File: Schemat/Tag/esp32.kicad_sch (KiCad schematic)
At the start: 30 parts, among them J4 Conn_01x02_Pin, J5 Conn_01x04_Pin, J6 Conn_01x02_Pin, J7 Conn_01x02_Pin, SW1 SW_Push, SW4 SW_Push, U7 ESP32-S3-WROOM-1

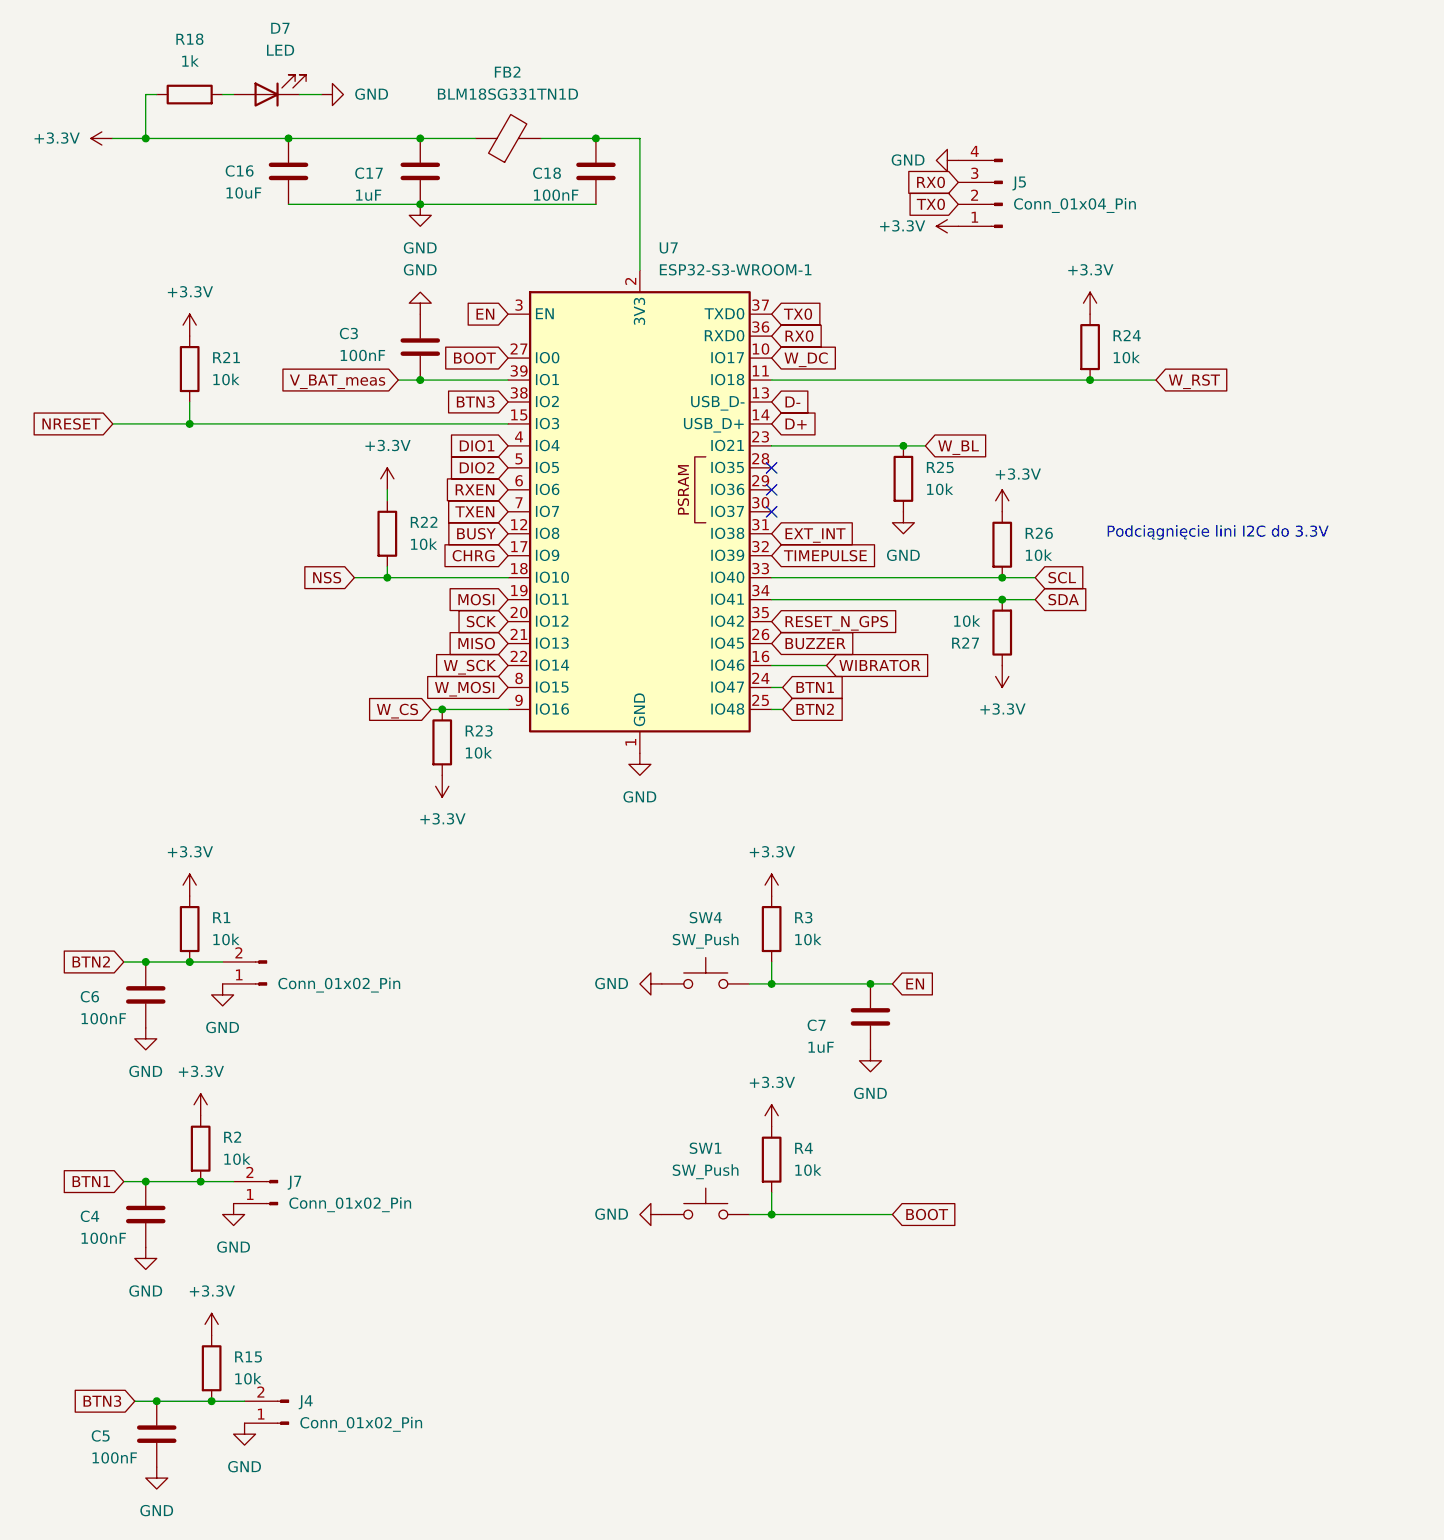
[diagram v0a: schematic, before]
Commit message: Poprawki 09.05
Zmiana poprowadzenia ścieżek sygnałowych w celu poprawy wylewki GND
Dodatkowe przelotki przy GND układy TPS631000
Dodanie zworek 0R z miedzią na wierzchu dla większości linii sygnałowych (nie dodano dla ścieżek do przycisków, bo tam są pady)
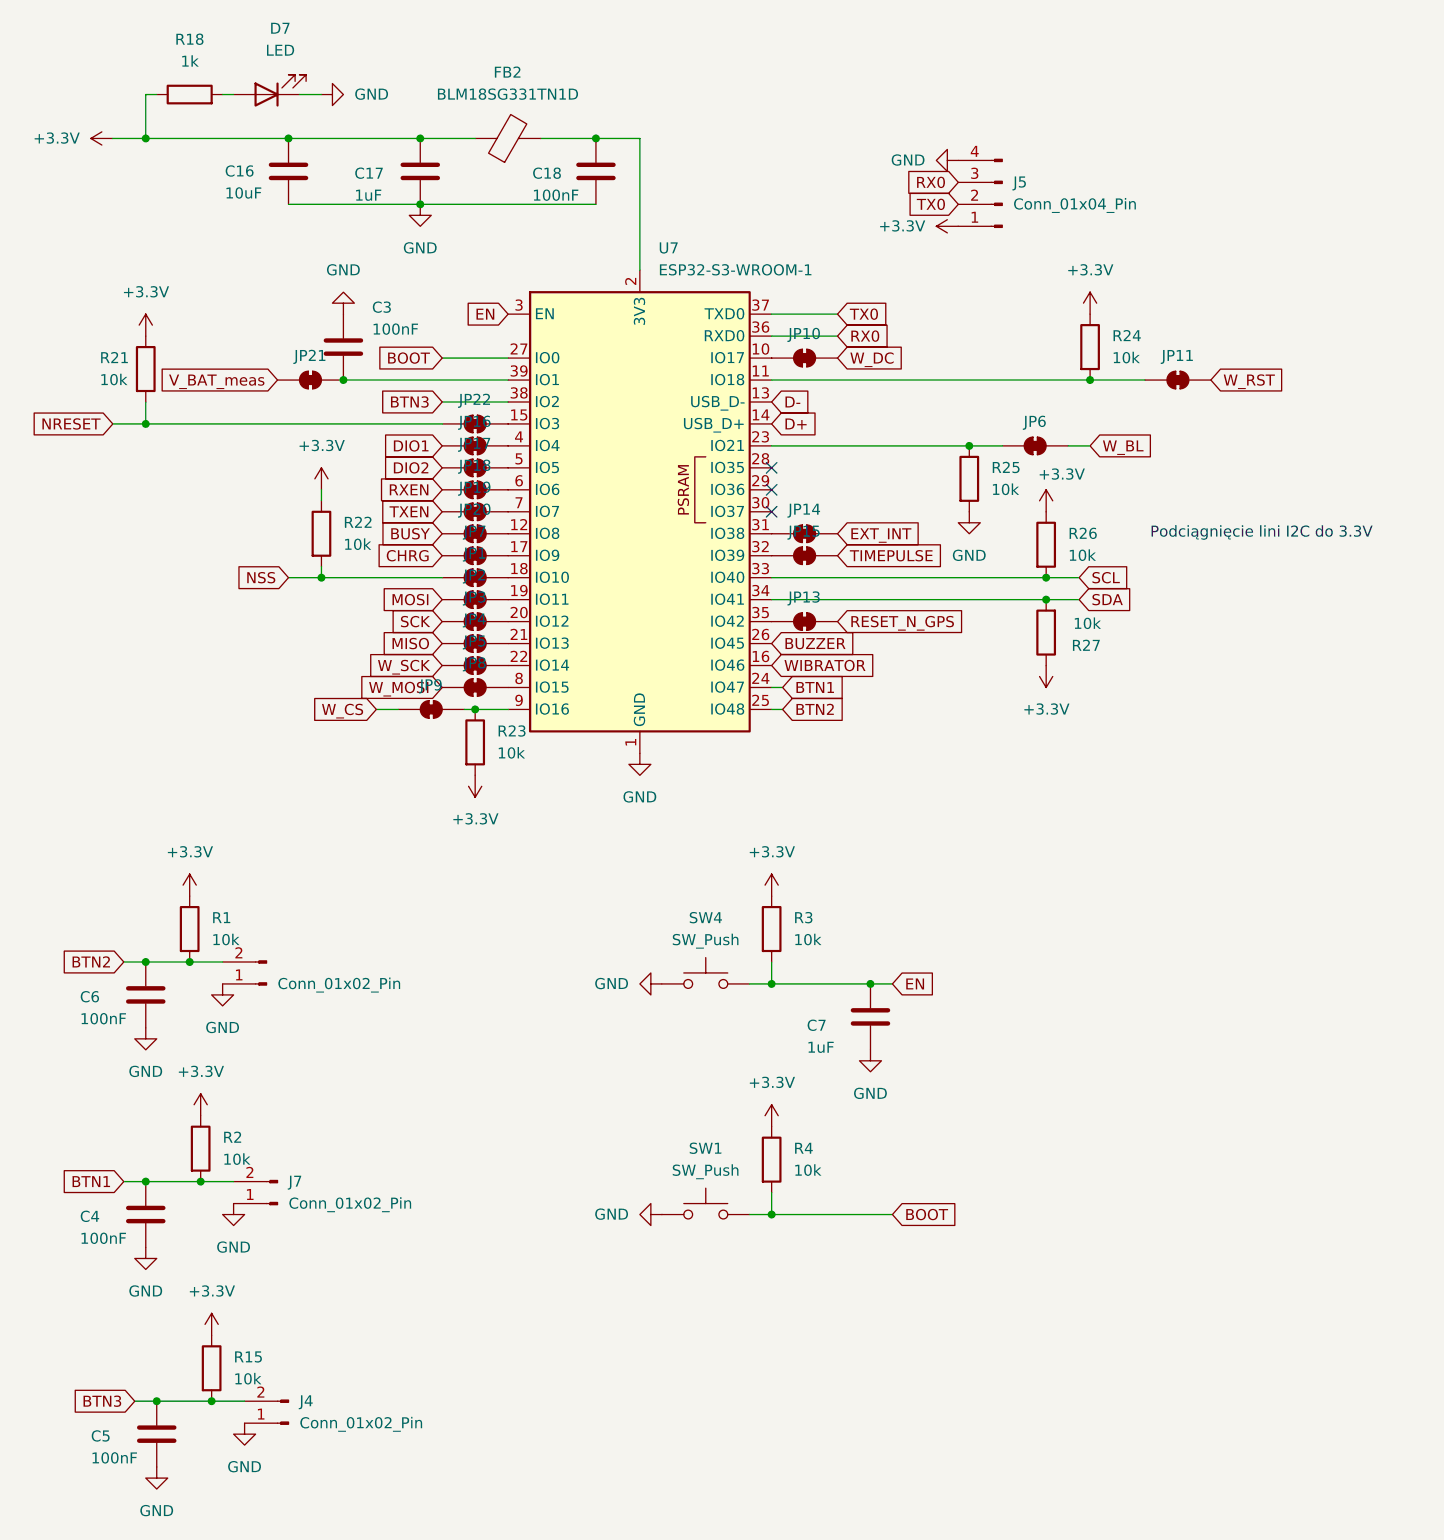
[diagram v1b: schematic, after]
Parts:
- added JP1, JP10, JP11, JP13, JP14, JP15, JP16, JP17, JP18, JP19, JP2, JP20, JP21, JP22, JP3, JP4, JP5, JP6, JP7, JP8, JP9: SolderJumper_2_Bridged, Biblioteka:Zworka, symbol Jumper:SolderJumper_2_Bridged
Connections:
- net BUSY: now also JP20.1 (A); no longer U7.12 (IO8)
- net CHRG: now also JP7.1 (A); no longer U7.17 (IO9)
- net DIO1: now also JP16.1 (A); no longer U7.4 (IO4)
- net DIO2: now also JP17.1 (A); no longer U7.5 (IO5)
- net EXT_INT: now also JP14.2 (B); no longer U7.31 (IO38)
- net MISO: now also JP4.1 (A); no longer U7.21 (IO13)
- net MOSI: now also JP2.1 (A); no longer U7.19 (IO11)
- net NRESET: now also JP22.1 (A); no longer U7.15 (IO3)
- net NSS: now also JP1.1 (A); no longer U7.18 (IO10)
- net RESET_N_GPS: now also JP13.2 (B); no longer U7.35 (IO42)
- net RXEN: now also JP18.1 (A); no longer U7.6 (IO6)
- net SCK: now also JP3.1 (A); no longer U7.20 (IO12)
- net TIMEPULSE: now also JP15.2 (B); no longer U7.32 (IO39)
- net TXEN: now also JP19.1 (A); no longer U7.7 (IO7)
- net V_BAT_meas: now also JP21.1 (A); no longer C3.1, U7.39 (IO1)
- net W_BL: now also JP6.2 (B); no longer R25.1, U7.23 (IO21)
- net W_CS: now also JP9.1 (A); no longer R23.1, U7.9 (IO16)
- net W_DC: now also JP10.2 (B); no longer U7.10 (IO17)
- net W_MOSI: now also JP8.1 (A); no longer U7.8 (IO15)
- net W_RST: now also JP11.2 (B); no longer R24.2, U7.11 (IO18)
- net W_SCK: now also JP5.1 (A); no longer U7.22 (IO14)
- new net: JP11.1 (A), R24.2, U7.11 (IO18)
- new net: JP19.2 (B), U7.7 (IO7)
- new net: JP9.2 (B), R23.1, U7.9 (IO16)
- new net: JP13.1 (A), U7.35 (IO42)
- new net: JP18.2 (B), U7.6 (IO6)
- new net: JP8.2 (B), U7.8 (IO15)
- new net: JP5.2 (B), U7.22 (IO14)
- new net: JP10.1 (A), U7.10 (IO17)
- new net: JP20.2 (B), U7.12 (IO8)
- new net: JP22.2 (B), U7.15 (IO3)
- new net: JP7.2 (B), U7.17 (IO9)
- new net: JP1.2 (B), U7.18 (IO10)
- new net: JP2.2 (B), U7.19 (IO11)
- new net: JP3.2 (B), U7.20 (IO12)
- new net: JP4.2 (B), U7.21 (IO13)
- new net: JP6.1 (A), R25.1, U7.23 (IO21)
- new net: JP14.1 (A), U7.31 (IO38)
- new net: JP15.1 (A), U7.32 (IO39)
- new net: C3.1, JP21.2 (B), U7.39 (IO1)
- new net: JP16.2 (B), U7.4 (IO4)
- new net: JP17.2 (B), U7.5 (IO5)
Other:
- moved on the sheet: C3, R21, R22, R23, R25, R26, R27
